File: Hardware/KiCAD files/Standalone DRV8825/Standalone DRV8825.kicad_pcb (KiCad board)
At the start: 2 copper layers, 35.6 x 26.7 mm, 15 parts, among them J10 PINHD_1x8_Male, J9 PINHD_1x8_Male, U5 DRV8825PWPR

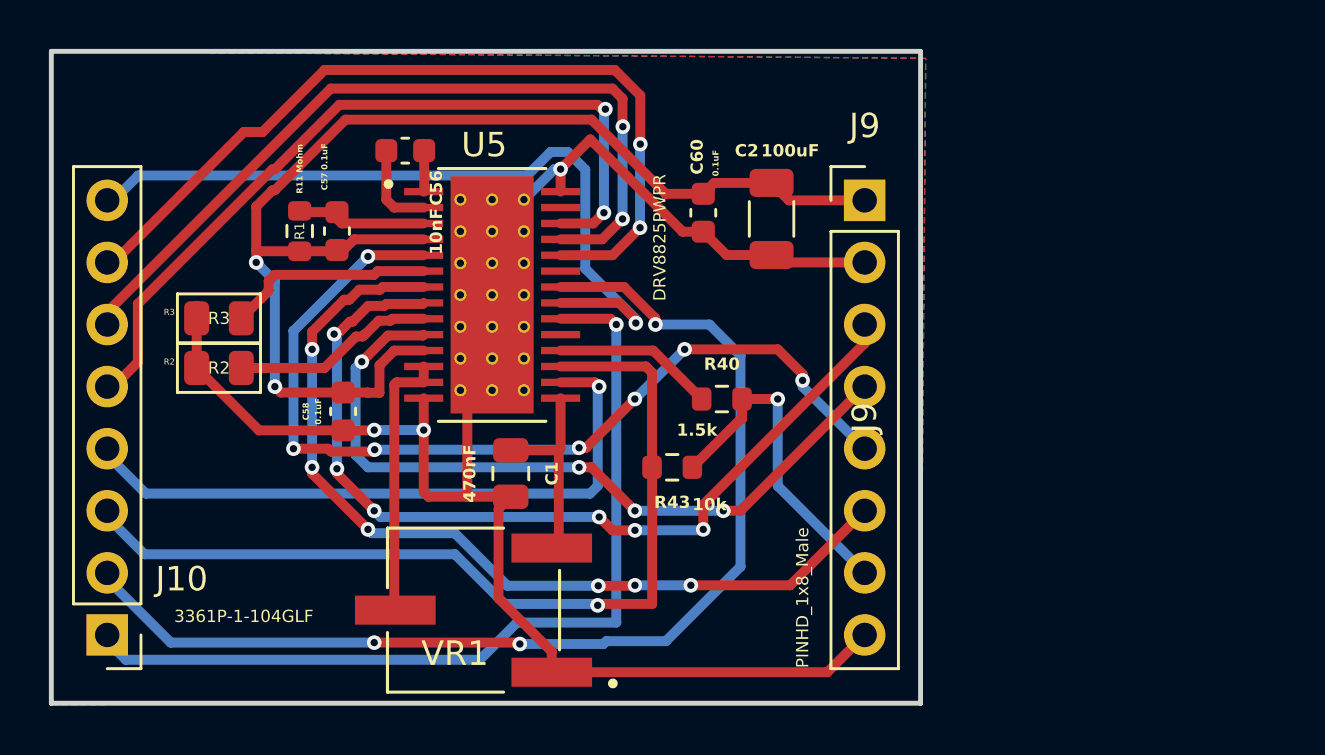
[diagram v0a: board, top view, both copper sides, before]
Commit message: general progress and adjustments
new footprint for pi reg inductor, var reg checked concurred with current part and value. re footprinted motor driver. started swapping head. adjusted some device footprints.
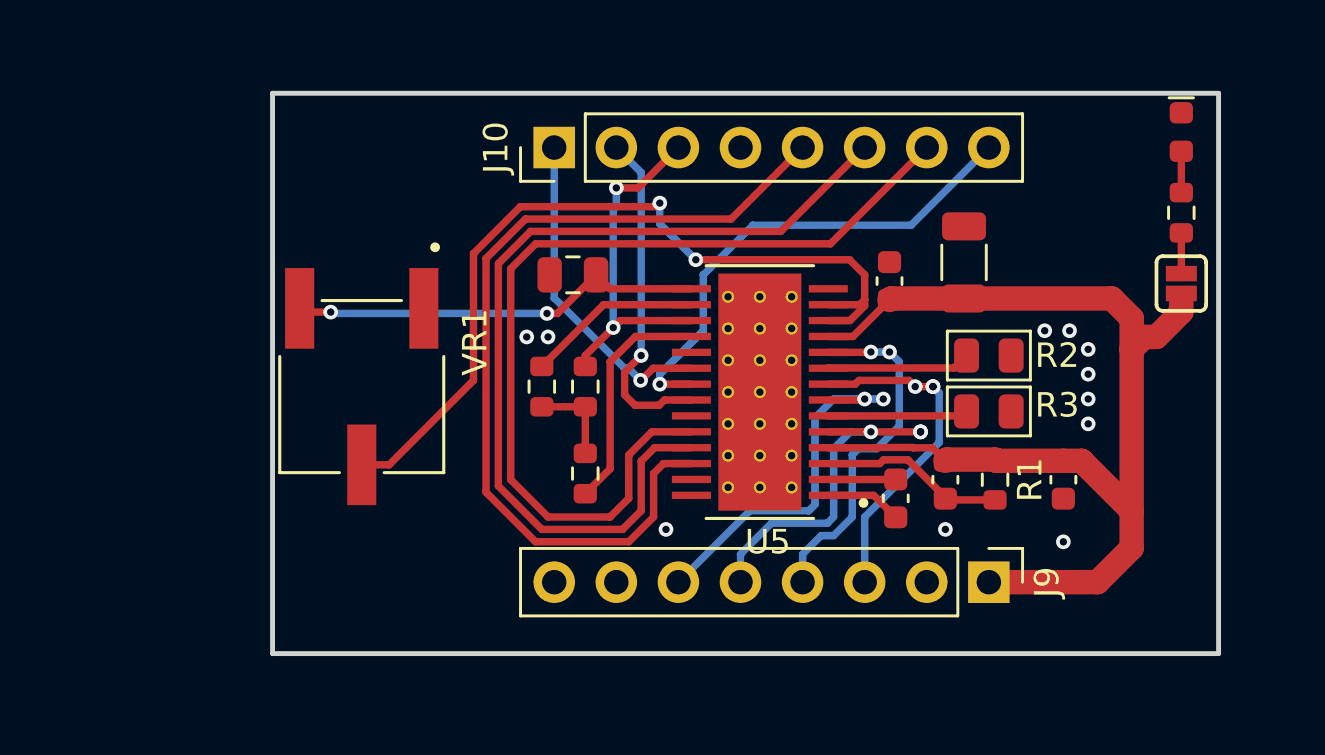
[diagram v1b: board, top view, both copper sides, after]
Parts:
- added D1: Blue, PCM_SparkFun-LED:LED_0603_1608Metric_Blue, F.Cu at (189.5, 59.4)
- added JP1: ~, PCM_SparkFun-Jumper:Jumper_2_NO, F.Cu at (189.5, 65.6)
- added R4: 2.2k, PCM_SparkFun-Resistor:R_0603_1608Metric, F.Cu at (189.5, 62.7)
- added R44: 10k, PCM_SparkFun-Resistor:R_0603_1608Metric, F.Cu at (163.3, 69.8)
- moved R3 31.7 mm to (181.6, 70.9), turned to 0 degrees
- moved R2 31.5 mm to (181.6, 68.6), turned to 0 degrees
- moved R1 30.2 mm to (181.9, 73.7), turned to -90 degrees
- moved C58 29.6 mm to (184.7, 73.7)
- moved J10 27.1 mm to (163.8, 60.1), turned to 90 degrees
- moved C57 26.9 mm to (179.8, 73.7), turned to 90 degrees
- moved C56 24.6 mm to (177.8, 74.4), turned to 90 degrees
- moved J9 16.4 mm to (181.6, 77.9), turned to -90 degrees
- moved U5 11.7 mm to (172.2, 70.1), turned to 180 degrees
- moved VR1 10.2 mm to (156.0, 69.8), turned to -90 degrees
- moved C1 8.52 mm to (164.6, 65.3), turned to 180 degrees
- moved C60 8.12 mm to (177.5, 65.5), turned to 90 degrees
- moved C2 8.07 mm to (180.6, 64.8), turned to 90 degrees
- moved R40 6.37 mm to (165.1, 73.4), turned to 90 degrees
- moved R43 4.85 mm to (165.1, 69.8), turned to 90 degrees
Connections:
- net Net-(U5-NRESET) renamed RESET
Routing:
- net GND: track 92.9 -> 0.00 mm, vias 3 -> 0
- net Net-(U5-STEP): track 45.6 -> 13.8 mm, vias 3 -> 1
- net /A1: track 38.6 -> 14.0 mm, vias 7 -> 3
- net /B2: track 37.0 -> 13.8 mm, vias 6 -> 3
- net Net-(U5-AVREF): track 11.1 -> 34.3 mm, vias 0 -> 2
- net Net-(U5-DIR): track 36.3 -> 13.4 mm
- net SLP: track 37.1 -> 14.4 mm, vias 1 -> 2
- net /A2: track 36.9 -> 15.1 mm, vias 6 -> 2
- net RESET: track 26.6 -> 7.17 mm, vias 1 -> 0
- net /B1: track 30.8 -> 14.5 mm, vias 4 -> 2
- net Net-(U5-NENBL): track 31.4 -> 20.3 mm
- net Net-(J9-Pad7): track 13.7 -> 3.68 mm, vias 1 -> 0
- net +3V3: track 8.24 -> 17.0 mm, vias 0 -> 2
- net +12V: track 50.4 -> 46.0 mm, vias 2 -> 0
- net Net-(U5-MODE1): track 33.6 -> 37.3 mm, vias 2 -> 0
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- removed copper zone on B.Cu, net GND
- removed copper zone on F.Cu, net GND
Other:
- board size 35.6 x 26.7 mm -> 38.7 x 22.9 mm

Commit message: general updates to the schematics and layouts
includes some backchecks tot he master schematic to be accurate for the paper
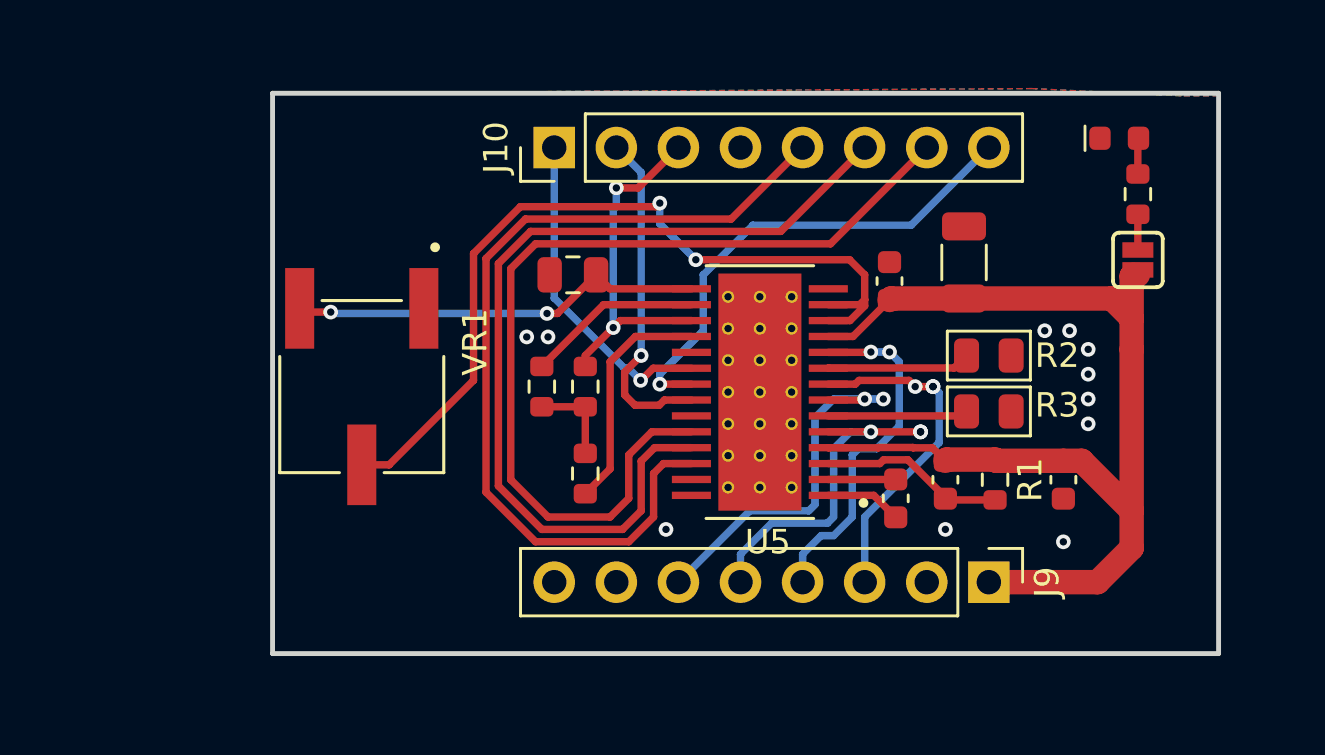
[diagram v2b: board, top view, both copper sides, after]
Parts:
- moved D1 2.55 mm to (186.9, 59.7), turned to 0 degrees
- moved JP1 2.02 mm to (187.7, 64.7)
- moved R4 1.93 mm to (187.7, 62.0)
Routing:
- net +12V: track 46.0 -> 44.7 mm
- net GND: vias 0 -> 11
- net (no net): vias 11 -> 0
- added copper zone on B.Cu, net GND
- added copper zone on F.Cu, net GND

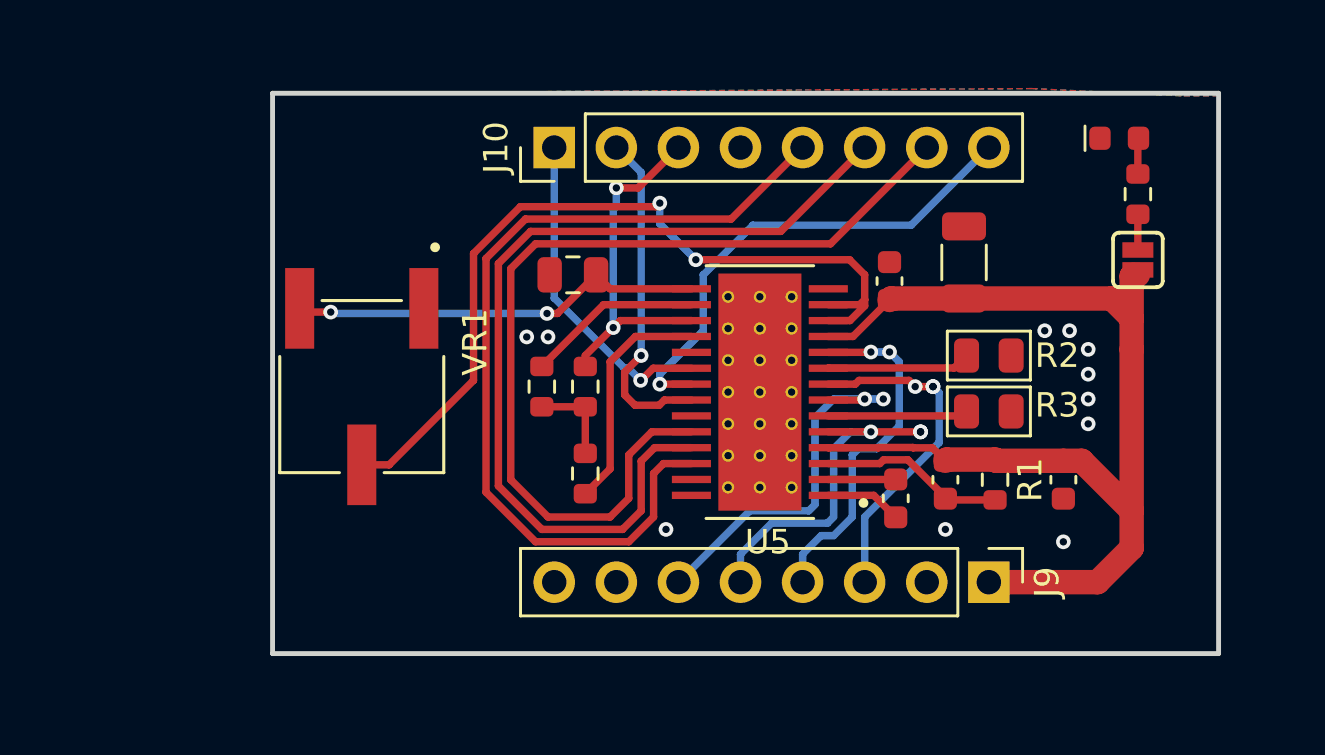
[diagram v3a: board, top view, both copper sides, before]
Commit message: part of the way through next iteration
Non-daisy chain Mainboard is ~50% through
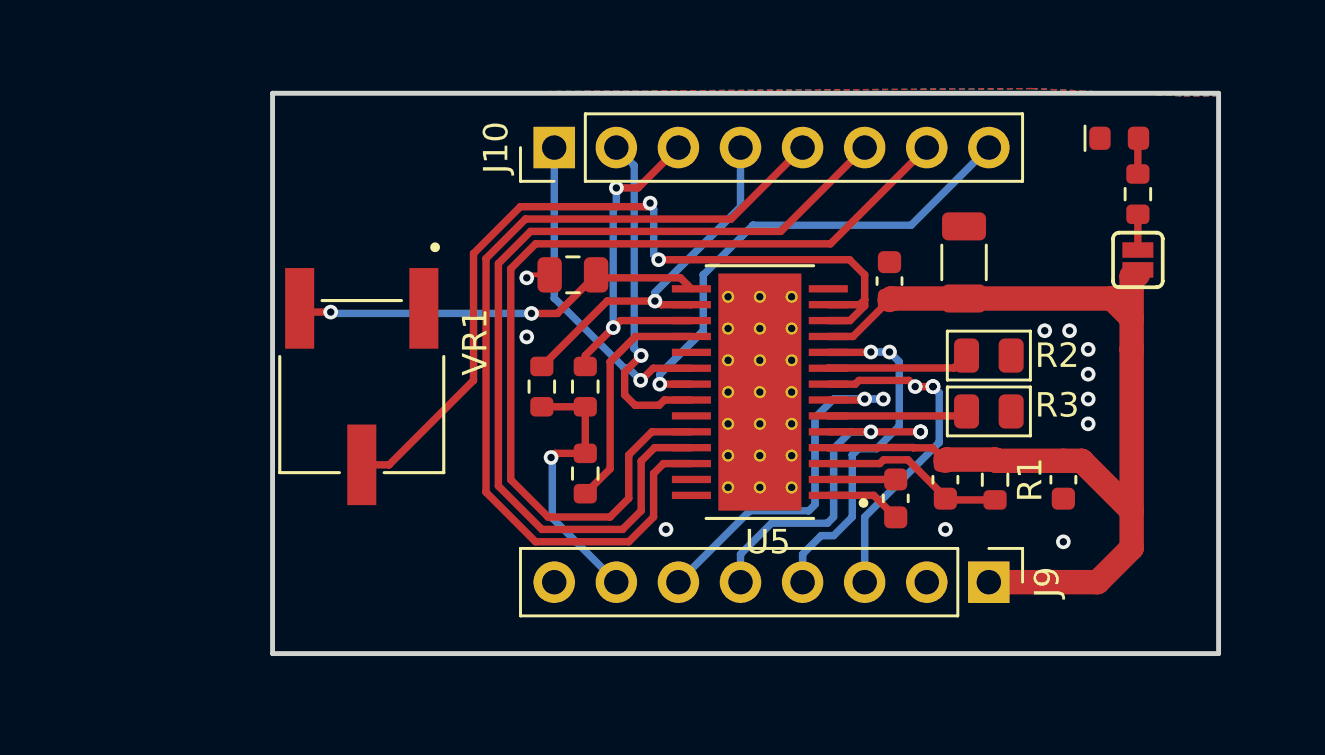
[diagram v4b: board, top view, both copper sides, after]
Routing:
- net RESET: track 7.17 -> 15.0 mm, vias 0 -> 1
- net Net-(J9-Pad7): track 3.68 -> 11.4 mm, vias 0 -> 1
- net GND: track 0.00 -> 0.99 mm
- net Net-(U5-AVREF): track 34.3 -> 35.0 mm

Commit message: 1st submitted iteration
added a folder for reviewing PCB's.
fixed various smaller issues on the PCB.
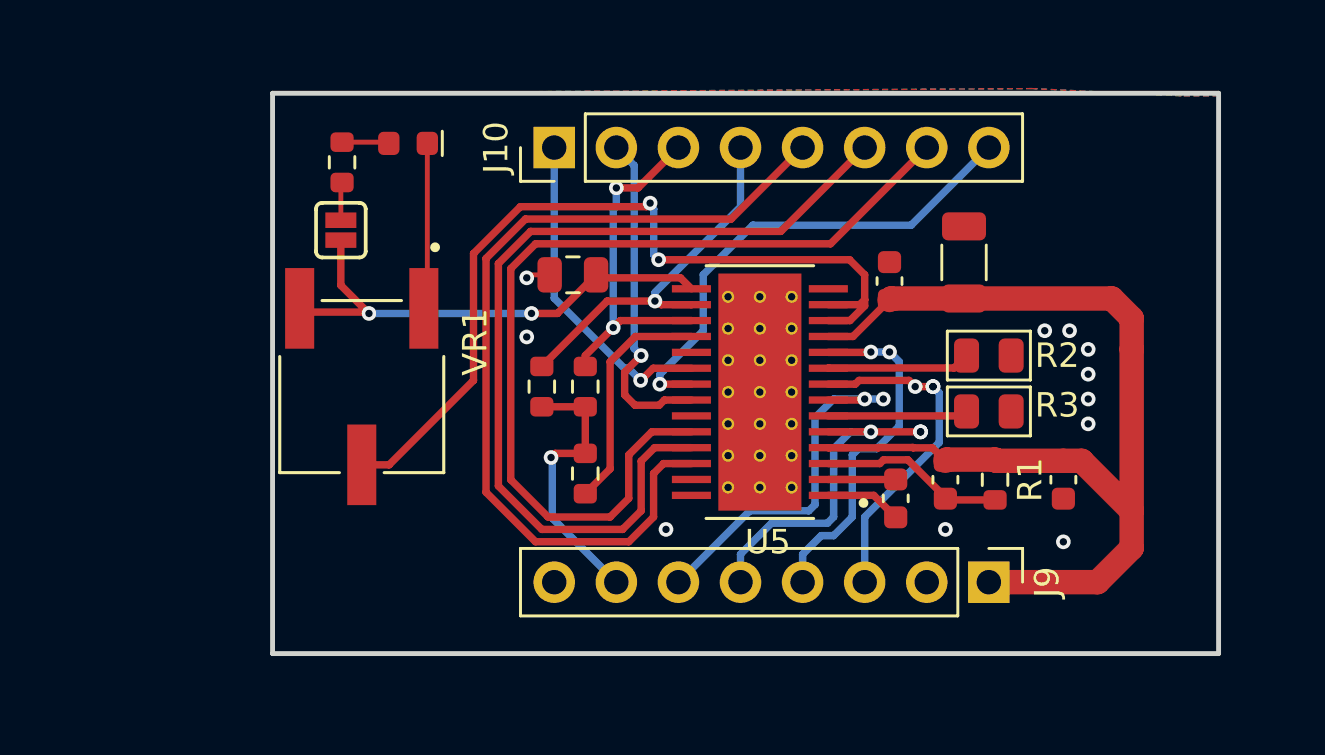
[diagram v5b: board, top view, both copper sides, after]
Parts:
- C2: value 100uF -> 3.3uF
- moved JP1 32.6 mm to (155.1, 63.5)
- moved R4 32.6 mm to (155.2, 60.7)
- moved D1 29.1 mm to (157.8, 59.9), turned to 180 degrees
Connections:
- JP1 pad 1: +12V -> +3V3
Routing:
- net GND: track 0.99 -> 7.80 mm
- net +3V3: track 17.0 -> 20.5 mm
- net +12V: track 44.7 -> 42.7 mm
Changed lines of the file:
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@@
 			)
 		)
-		(property "Value" "100uF"
+		(property "Value" "3.3uF"
 			(at 0 1.85 90)
 			(layer "F.Fab")
@@
 	(footprint "PCM_SparkFun-LED:LED_0603_1608Metric_Blue"
 		(layer "F.Cu")
-		(at 186.944 59.69)
+		(at 157.85 59.9 180)
 		(tags "SparkFun LED")
 		(property "Reference" "D1"
@@
 		)
 		(property "Datasheet" "https://media.digikey.com/pdf/Data%20Sheets/Rohm%20PDFs/SMLE12_Series_Rev2.0_2007.pdf"
-			(at 0 0 0)
+			(at 0 0 180)
 			(unlocked yes)
 			(layer "F.Fab")
@@
 		)
 		(property "Description" "Light emitting diode"
-			(at 0 0 0)
+			(at 0 0 180)
 			(unlocked yes)
 			(layer "F.Fab")
@@
 		)
 		(property "PROD_ID" "DIO-08575"
-			(at 0 0 0)
+			(at 0 0 180)
 			(unlocked yes)
 			(layer "F.Fab")
@@
 		)
 		(fp_line
-			(start -1.48 -0.73)
-			(end 1.48 -0.73)
+			(start 1.48 0.73)
+			(end -1.48 0.73)
 			(stroke
 				(width 0.05)
@@
 		)
 		(fp_line
-			(start -1.48 0.73)
-			(end -1.48 -0.73)
+			(start 1.48 -0.73)
+			(end 1.48 0.73)
 			(stroke
 				(width 0.05)
@@
 		)
 		(fp_line
-			(start 1.48 -0.73)
-			(end 1.48 0.73)
+			(start -1.48 0.73)
+			(end -1.48 -0.73)
 			(stroke
 				(width 0.05)
@@
 		)
 		(fp_line
-			(start 1.48 0.73)
-			(end -1.48 0.73)
+			(start -1.48 -0.73)
+			(end 1.48 -0.73)
 			(stroke
 				(width 0.05)
@@
 		)
 		(fp_line
-			(start -0.8 -0.1)
-			(end -0.8 0.4)
+			(start 0.8 0.4)
+			(end 0.8 -0.4)
 			(stroke
 				(width 0.1)
@@
 		)
 		(fp_line
-			(start -0.8 0.4)
-			(end 0.8 0.4)
+			(start 0.8 -0.4)
+			(end -0.5 -0.4)
 			(stroke
 				(width 0.1)
@@
 		)
 		(fp_line
-			(start 0.8 -0.4)
-			(end -0.5 -0.4)
+			(start -0.8 0.4)
+			(end 0.8 0.4)
 			(stroke
 				(width 0.1)
@@
 		)
 		(fp_line
-			(start 0.8 0.4)
-			(end 0.8 -0.4)
+			(start -0.8 -0.1)
+			(end -0.8 0.4)
 			(stroke
 				(width 0.1)
@@
 		)
 		(pad "1" smd roundrect
-			(at -0.7875 0)
+			(at -0.7875 0 180)
 			(size 0.875 0.95)
 			(layers "F.Cu" "F.Mask" "F.Paste")
@@
 		)
 		(pad "2" smd roundrect
-			(at 0.7875 0)
+			(at 0.7875 0 180)
 			(size 0.875 0.95)
 			(layers "F.Cu" "F.Mask" "F.Paste")
@@
 	(footprint "PCM_SparkFun-Resistor:R_0603_1608Metric"
 		(layer "F.Cu")
-		(at 187.706 61.976 90)
+		(at 155.15 60.675 90)
 		(descr "Resistor SMD 0603 (1608 Metric), square (rectangular) end terminal, IPC_7351 nominal, (Body size source: IPC-SM-782 page 72, https://www.pcb-3d.com/wordpress/wp-content/uploads/ipc-sm-782a_amendment_1_and_2.pdf), generated with kicad-footprint-generator")
 		(tags "SparkFun resistor")
@@
 	(footprint "PCM_SparkFun-Jumper:Jumper_2_NO"
 		(layer "F.Cu")
-		(at 187.706 64.6684 90)
+		(at 155.1 63.45 90)
 		(tags "SparkFun")
 		(property "Reference" "JP1"
@@
 			(size 0.635 1.27)
 			(layers "F.Cu" "F.Mask")
-			(net "+12V")
+			(net "+3V3")
 			(pinfunction "A_1")
 			(pintype "passive")
@@
 	)
 	(segment
-		(start 187.5013 65.2795)
-		(end 187.706 65.2795)
-		(width 1)
-		(layer "F.Cu")
-		(net "+12V")
-	)
-	(segment
 		(start 175.042 67.799)
 		(end 176.054 67.799)
@@
 	)
 	(segment
-		(start 187.452 67.056)
-		(end 187.452 65.3288)
-		(width 1)
-		(layer "F.Cu")
-		(net "+12V")
-	)
-	(segment
 		(start 186.055 77.851)
 		(end 187.452 76.454)
@@
 	)
 	(segment
-		(start 187.452 65.3288)
-		(end 187.5013 65.2795)
-		(width 1)
-		(layer "F.Cu")
-		(net "+12V")
-	)
-	(segment
 		(start 179.3008 72.3538)
 		(end 179.832 72.885)
@@
 	)
 	(segment
+		(start 158.6375 59.9)
+		(end 158.6375 66.5085)
+		(width 0.2)
+		(layer "F.Cu")
+		(net "GND")
+	)
+	(segment
+		(start 158.6375 66.5085)
+		(end 158.496 66.65)
+		(width 0.2)
+		(layer "F.Cu")
+		(net "GND")
+	)
+	(segment
 		(start 162.8264 65.278)
 		(end 162.7044 65.4)
@@
 	)
 	(segment
-		(start 154.686 66.802)
-		(end 153.568 66.802)
+		(start 153.568 66.802)
+		(end 153.416 66.65)
 		(width 0.3048)
 		(layer "F.Cu")
@@
 	)
 	(segment
+		(start 156.25 66.857)
+		(end 155.1 65.707)
+		(width 0.3048)
+		(layer "F.Cu")
+		(net "+3V3")
+	)
+	(segment
+		(start 156.195 66.802)
+		(end 153.568 66.802)
+		(width 0.3048)
+		(layer "F.Cu")
+		(net "+3V3")
+	)
+	(segment
 		(start 165.664 65.4)
 		(end 165.542 65.278)
@@
 	)
 	(segment
-		(start 153.568 66.802)
-		(end 153.416 66.65)
+		(start 155.1 65.707)
+		(end 155.1 63.8564)
+		(width 0.3048)
+		(layer "F.Cu")
+		(net "+3V3")
+	)
+	(segment
+		(start 156.25 66.857)
+		(end 156.195 66.802)
 		(width 0.3048)
 		(layer "F.Cu")
@@
 	)
 	(via
-		(at 154.686 66.802)
+		(at 156.25 66.857)
 		(size 0.6)
 		(drill 0.3)
@@
 	)
 	(segment
-		(start 162.9 66.857)
-		(end 154.741 66.857)
-		(width 0.3048)
-		(layer "B.Cu")
-		(net "+3V3")
-	)
-	(segment
-		(start 154.741 66.857)
-		(end 154.686 66.802)
+		(start 156.25 66.857)
+		(end 162.9 66.857)
 		(width 0.3048)
 		(layer "B.Cu")
@@
 	)
 	(segment
-		(start 187.706 59.7155)
-		(end 187.7315 59.69)
-		(width 0.3048)
+		(start 157.0125 59.85)
+		(end 157.0625 59.9)
+		(width 0.2)
 		(layer "F.Cu")
 		(net "Net-(D1-A)")
 	)
 	(segment
-		(start 187.706 61.151)
-		(end 187.706 59.7155)
-		(width 0.3048)
+		(start 155.15 59.85)
+		(end 157.0125 59.85)
+		(width 0.2)
 		(layer "F.Cu")
 		(net "Net-(D1-A)")
 	)
 	(segment
-		(start 187.706 64.262)
-		(end 187.706 62.801)
-		(width 0.3048)
+		(start 155.1 61.55)
+		(end 155.15 61.5)
+		(width 0.2)
+		(layer "F.Cu")
+		(net "Net-(JP1-B)")
+	)
+	(segment
+		(start 155.1 63.0436)
+		(end 155.1 61.55)
+		(width 0.2)
 		(layer "F.Cu")
 		(net "Net-(JP1-B)")

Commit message: sick weekend changes
small adjustments left our some larger protection changes till after talking to weeks
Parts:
- removed JP1: ~, PCM_SparkFun-Jumper:Jumper_2_NO
- added R5: 0, Resistor_SMD:R_0805_2012Metric, F.Cu at (155.9, 63.8)
- R4: footprint PCM_SparkFun-Resistor:R_0603_1608Metric -> Resistor_SMD:R_0805_2012Metric
- moved C2 4.27 mm to (184.8, 65.0)
- moved J10 3.03 mm to (163.8, 63.1)
- moved R40 1.73 mm to (164.3, 71.8), turned to 180 degrees
- moved C60 0.87 mm to (177.5, 66.4)
- moved J9 0.80 mm to (181.6, 77.0)
- moved C1 0.77 mm to (164.6, 66.0)
- moved R44 0.45 mm to (163.3, 69.4)
- moved R43 0.45 mm to (165.1, 69.4)
- moved C56 0.23 mm to (177.6, 74.3), turned to 180 degrees
- moved R4 0.18 mm to (155.2, 60.9)
- moved C57 0.13 mm to (179.9, 73.5)
- moved C58 0.11 mm to (184.7, 73.5)
- moved R1 0.11 mm to (181.9, 73.5)
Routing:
- net GND: track 7.80 -> 39.8 mm, vias 11 -> 8
- net Net-(U5-AVREF): track 35.0 -> 27.0 mm
- net SLP: track 14.4 -> 10.5 mm, vias 2 -> 1
- net Net-(U5-STEP): track 13.8 -> 10.8 mm
- net Net-(U5-DIR): track 13.4 -> 10.4 mm
- net RESET: track 15.0 -> 12.1 mm
- net /A1: track 14.0 -> 11.2 mm, vias 3 -> 1
- net Net-(U5-NFAULT): track 9.57 -> 7.16 mm
- net Net-(U5-MODE2): track 36.0 -> 38.3 mm, vias 0 -> 1
- net Net-(U5-MODE0): track 38.2 -> 39.9 mm, vias 0 -> 1
- net Net-(R4-Pad1): track 1.56 -> 2.70 mm
- net Net-(U5-NENBL): track 20.3 -> 19.3 mm
- net Net-(J9-Pad7): track 11.4 -> 10.4 mm
- net Net-(U5-CP1): track 3.13 -> 4.02 mm
- net +3V3: track 20.5 -> 21.4 mm
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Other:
- board size 38.7 x 22.9 mm -> 38.7 x 23.3 mm
